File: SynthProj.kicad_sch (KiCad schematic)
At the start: 38 parts, among them J18 Ext In, J29 Conn_01x16_Pin, SW5 SW_DPDT_x2

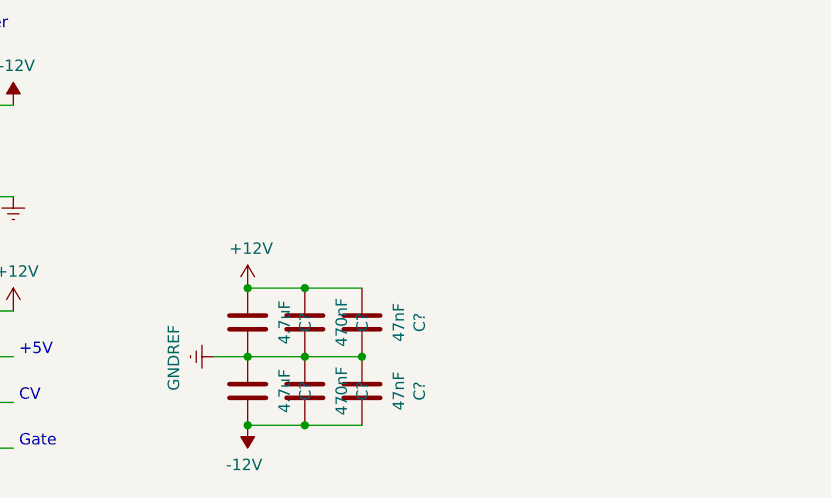
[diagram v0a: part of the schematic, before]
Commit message: added manufacturing files
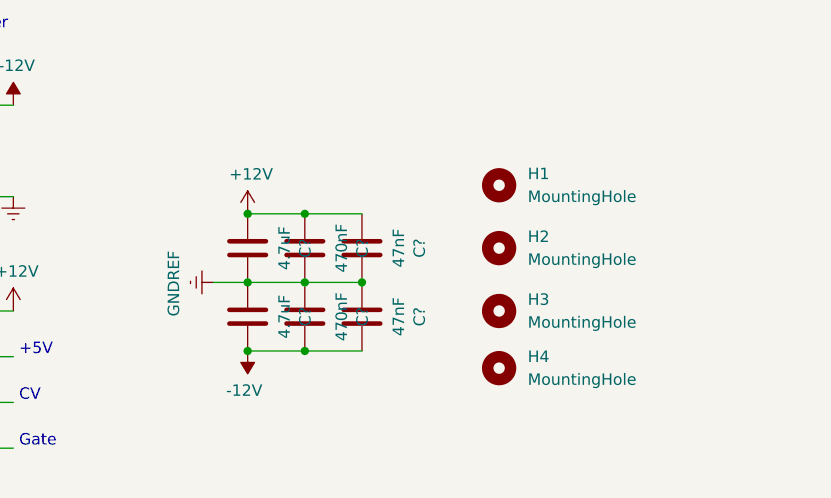
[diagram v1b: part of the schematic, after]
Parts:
- added H1, H2, H3, H4: MountingHole, MountingHole:MountingHole_3.2mm_M3_Pad, symbol Mechanical:MountingHole
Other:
- moved on the sheet: C?
